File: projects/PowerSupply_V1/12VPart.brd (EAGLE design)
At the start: 49.5 x 58.4 mm, 24 parts, among them IC1 LM2596T, IC2 LM2596T, X1 IN, X2 OUT

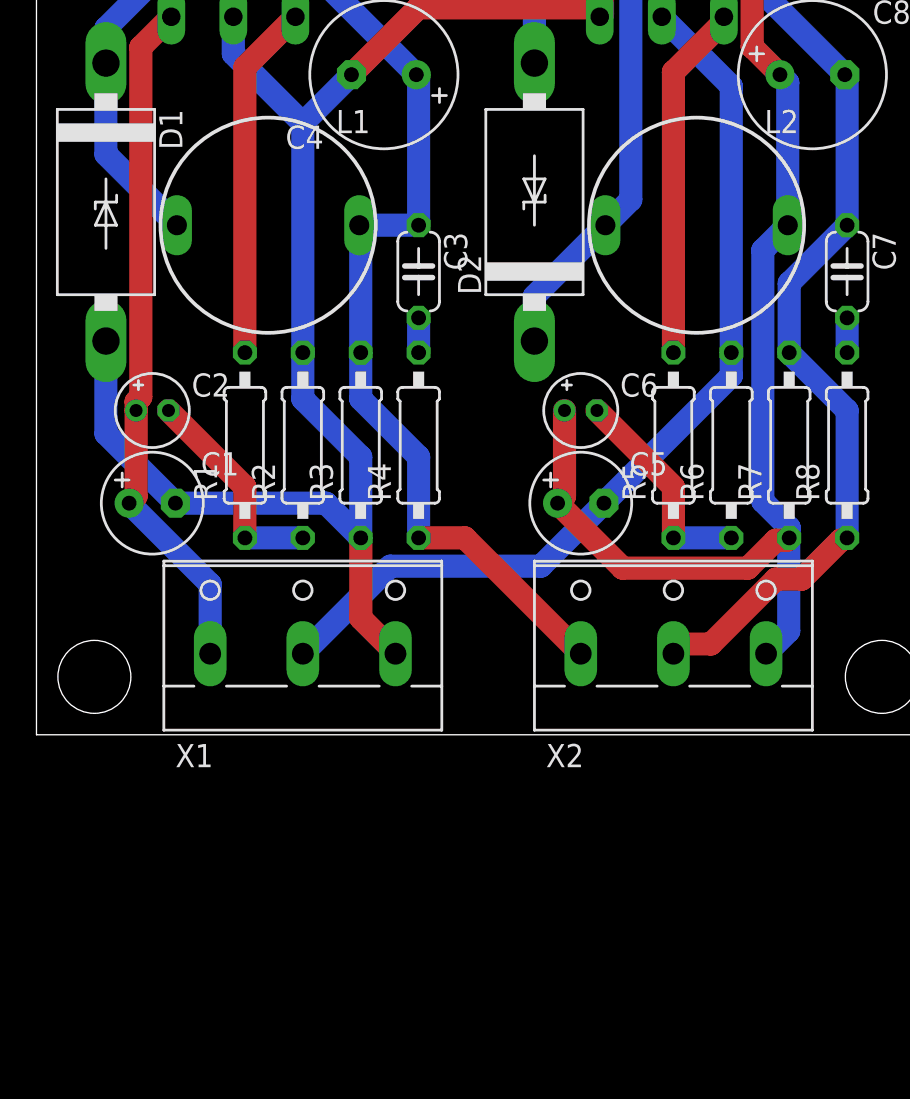
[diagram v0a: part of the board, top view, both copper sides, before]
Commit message: refactor(12v): schematics changed
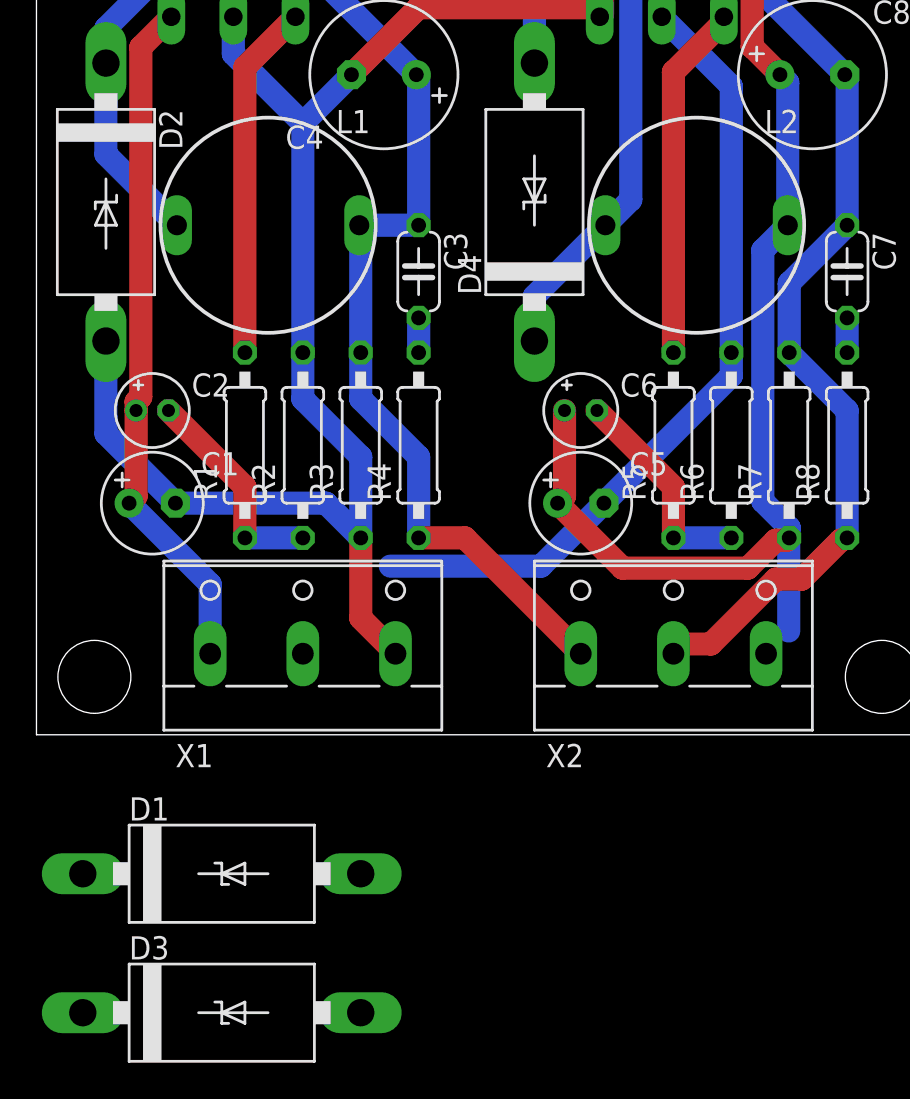
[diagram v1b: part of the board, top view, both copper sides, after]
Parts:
- added D3, D4: 1N5822, diode:C4111-15
- moved D1 37.4 mm to (10.2, -7.62), turned to 0 degrees
- moved D2 23.5 mm to (3.81, 29.2), turned to 270 degrees
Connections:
- net +24V: now also D1.C
- net -12V: now also D4.A, X2.3; no longer D2.A, X2.2
- net -24V: now also D3.C, X1.3; no longer X1.2
- net GND: now also D2.A, D3.A, X1.2, X2.2; no longer X1.3, X2.3
- net N$2: now also D4.C; no longer D2.C
- net N$3: now also D2.C; no longer D1.C
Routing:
- net -24V: track 51.1 -> 44.3 mm
- net GND: track 155.8 -> 154.0 mm
- net -12V: track 67.5 -> 66.8 mm
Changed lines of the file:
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@@
 <attribute name="VALUE" x="40.259" y="33.147" size="1.27" layer="27" ratio="10"/>
 </element>
-<element name="D1" library="diode" library_urn="urn:adsk.eagle:library:210" package="C4111-15" package3d_urn="urn:adsk.eagle:package:43355/2" value="1N5822" x="3.81" y="29.21" smashed="yes" rot="R270">
+<element name="D2" library="diode" library_urn="urn:adsk.eagle:library:210" package="C4111-15" package3d_urn="urn:adsk.eagle:package:43355/2" value="1N5822" x="3.81" y="29.21" smashed="yes" rot="R270">
 <attribute name="NAME" x="6.731" y="34.29" size="1.27" layer="25" ratio="10" rot="R270"/>
 <attribute name="POPULARITY" value="0" x="-25.4" y="-16.51" size="1.778" layer="27" rot="R270" display="off"/>
 <attribute name="VALUE" x="1.651" y="31.75" size="1.27" layer="27" ratio="10" rot="R270"/>
 </element>
-<element name="D2" library="diode" library_urn="urn:adsk.eagle:library:210" package="C4111-15" package3d_urn="urn:adsk.eagle:package:43355/2" value="1N5822" x="27.305" y="29.21" smashed="yes" rot="R90">
+<element name="D4" library="diode" library_urn="urn:adsk.eagle:library:210" package="C4111-15" package3d_urn="urn:adsk.eagle:package:43355/2" value="1N5822" x="27.305" y="29.21" smashed="yes" rot="R90">
 <attribute name="NAME" x="24.384" y="24.13" size="1.27" layer="25" ratio="10" rot="R90"/>
 <attribute name="POPULARITY" value="0" x="65.405" y="52.07" size="1.778" layer="27" rot="R90" display="off"/>
@@
 <attribute name="VALUE" x="28.321" y="0.762" size="1.27" layer="27" ratio="10"/>
 </element>
+<element name="D1" library="diode" library_urn="urn:adsk.eagle:library:210" package="C4111-15" package3d_urn="urn:adsk.eagle:package:43355/2" value="1N5822" x="10.16" y="-7.62" smashed="yes">
+<attribute name="NAME" x="5.08" y="-4.699" size="1.27" layer="25" ratio="10"/>
+<attribute name="POPULARITY" value="0" x="10.16" y="-7.62" size="1.778" layer="27" display="off"/>
+<attribute name="VALUE" x="7.62" y="-9.779" size="1.27" layer="27" ratio="10"/>
+</element>
+<element name="D3" library="diode" library_urn="urn:adsk.eagle:library:210" package="C4111-15" package3d_urn="urn:adsk.eagle:package:43355/2" value="1N5822" x="10.16" y="-15.24" smashed="yes">
+<attribute name="NAME" x="5.08" y="-12.319" size="1.27" layer="25" ratio="10"/>
+<attribute name="POPULARITY" value="0" x="10.16" y="-15.24" size="1.778" layer="27" display="off"/>
+<attribute name="VALUE" x="7.62" y="-17.399" size="1.27" layer="27" ratio="10"/>
+</element>
 </elements>
 <signals>
 <signal name="GND">
-<contactref element="X1" pad="3"/>
 <contactref element="C1" pad="-"/>
 <contactref element="IC1" pad="3"/>
 <contactref element="R2" pad="2"/>
 <contactref element="R3" pad="1"/>
-<contactref element="D1" pad="A"/>
-<contactref element="X2" pad="3"/>
+<contactref element="D2" pad="A"/>
 <contactref element="L2" pad="2"/>
 <contactref element="R7" pad="1"/>
@@
 <contactref element="C6" pad="+"/>
 <contactref element="IC2" pad="1"/>
-<wire x1="40.005" y1="4.445" x2="41.2496" y2="5.6896" width="1.27" layer="16"/>
 <wire x1="17.78" y1="6.4008" x2="17.78" y2="10.795" width="1.27" layer="1"/>
-<wire x1="19.685" y1="4.445" x2="19.685" y2="4.4958" width="1.27" layer="1"/>
 <wire x1="19.685" y1="4.4958" x2="17.78" y2="6.4008" width="1.27" layer="1"/>
 <wire x1="40.5384" y1="10.668" x2="41.148" y2="10.668" width="1.27" layer="1"/>
@@
 <wire x1="31.0388" y1="39.5224" x2="31.0388" y2="44.9393875" width="1.27" layer="1"/>
 <wire x1="31.9464125" y1="45.847" x2="36.6335875" y2="45.847" width="1.27" layer="1"/>
+<contactref element="X1" pad="2"/>
+<contactref element="X2" pad="2"/>
+<contactref element="D1" pad="A"/>
+<contactref element="D3" pad="A"/>
+<wire x1="41.2496" y1="5.6896" x2="34.925" y2="4.445" width="0" layer="19" extent="16-16"/>
+<wire x1="14.605" y1="4.445" x2="19.685" y2="4.4958" width="0" layer="19" extent="1-1"/>
+<wire x1="17.78" y1="-7.62" x2="19.685" y2="4.4958" width="0" layer="19" extent="1-1"/>
+<wire x1="17.78" y1="-15.24" x2="17.78" y2="-7.62" width="0" layer="19" extent="1-1"/>
 </signal>
 <signal name="N$3">
 <contactref element="IC1" pad="2"/>
-<contactref element="D1" pad="C"/>
+<contactref element="D2" pad="C"/>
 <contactref element="L1" pad="1"/>
 <wire x1="7.7" y1="27.94" x2="3.81" y2="31.83" width="1.27" layer="16"/>
@@
 <contactref element="L2" pad="1"/>
 <contactref element="IC2" pad="2"/>
-<contactref element="D2" pad="C"/>
+<contactref element="D4" pad="C"/>
 <wire x1="31.195" y1="27.94" x2="27.305" y2="24.05" width="1.27" layer="16"/>
 <wire x1="27.305" y1="24.05" x2="27.305" y2="21.59" width="1.27" layer="16"/>
@@
 </signal>
 <signal name="-12V">
-<contactref element="X2" pad="2"/>
 <contactref element="C8" pad="-"/>
 <contactref element="IC2" pad="4"/>
@@
 <contactref element="R8" pad="1"/>
 <contactref element="C7" pad="1"/>
-<contactref element="D2" pad="A"/>
+<contactref element="D4" pad="A"/>
 <wire x1="40.5384" y1="8.5344" x2="36.9824" y2="4.9784" width="1.27" layer="1"/>
 <wire x1="41.9608" y1="8.5344" x2="40.5384" y2="8.5344" width="1.27" layer="1"/>
@@
 <wire x1="44.0944" y1="10.668" x2="44.45" y2="10.795" width="1.27" layer="1"/>
 <wire x1="36.9824" y1="4.9784" x2="35.4584" y2="4.9784" width="1.27" layer="1"/>
-<wire x1="35.4584" y1="4.9784" x2="34.925" y2="4.445" width="1.27" layer="1"/>
 <wire x1="27.305" y1="36.83" x2="27.305" y2="41.2055875" width="1.27" layer="16"/>
 <wire x1="27.305" y1="41.2055875" x2="31.9464125" y2="45.847" width="1.27" layer="16"/>
@@
 <wire x1="41.275" y1="20.955" x2="44.45" y2="17.78" width="1.27" layer="16"/>
 <wire x1="44.45" y1="17.78" x2="44.45" y2="10.795" width="1.27" layer="16"/>
+<contactref element="X2" pad="3"/>
+<wire x1="35.4584" y1="4.9784" x2="40.005" y2="4.445" width="0" layer="19" extent="1-1"/>
 </signal>
 <signal name="+24V">
@@
 <wire x1="5.08" y1="12.7" x2="9.525" y2="8.255" width="1.27" layer="16"/>
 <wire x1="9.525" y1="8.255" x2="9.525" y2="4.445" width="1.27" layer="16"/>
+<contactref element="D1" pad="C"/>
+<wire x1="2.54" y1="-7.62" x2="9.525" y2="4.445" width="0" layer="19" extent="1-1"/>
 </signal>
 <signal name="-24V">
-<contactref element="X1" pad="2"/>
 <contactref element="C5" pad="-"/>
 <contactref element="R6" pad="2"/>
 <contactref element="IC2" pad="3"/>
 <wire x1="19.4056" y1="9.2456" x2="27.6606" y2="9.2456" width="1.27" layer="16"/>
-<wire x1="19.4056" y1="9.2456" x2="14.605" y2="4.445" width="1.27" layer="16"/>
 <wire x1="31.115" y1="12.7" x2="38.1" y2="19.685" width="1.27" layer="16"/>
 <wire x1="38.1" y1="19.685" x2="38.1" y2="20.955" width="1.27" layer="16"/>
@@
 <wire x1="34.29" y1="39.37" x2="38.1" y2="35.56" width="1.27" layer="16"/>
 <wire x1="38.1" y1="35.56" x2="38.1" y2="20.955" width="1.27" layer="16"/>
+<contactref element="X1" pad="3"/>
+<contactref element="D3" pad="C"/>
+<wire x1="19.685" y1="4.445" x2="19.4056" y2="9.2456" width="0" layer="19" extent="16-16"/>
+<wire x1="2.54" y1="-15.24" x2="19.685" y2="4.445" width="0" layer="19" extent="1-1"/>
 </signal>
 <signal name="N$4">

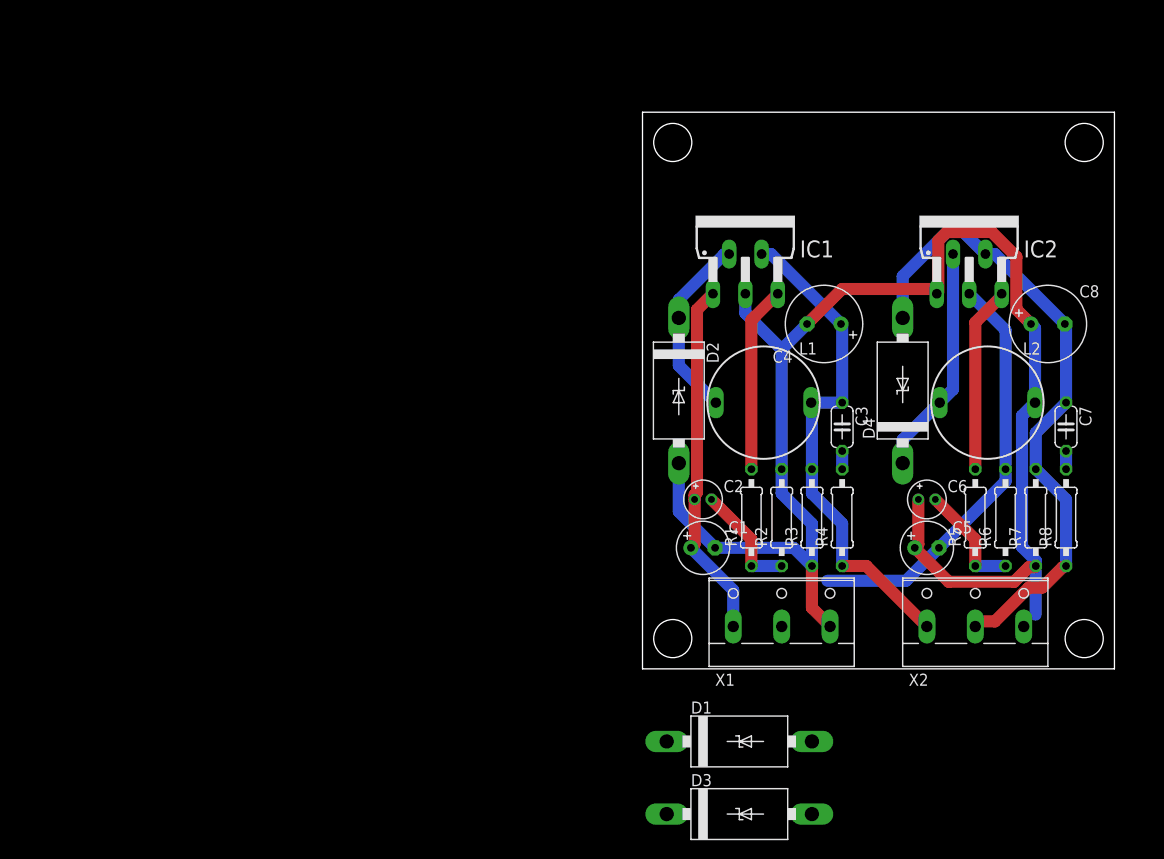
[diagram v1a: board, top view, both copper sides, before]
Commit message: refactor(1v): routing changed
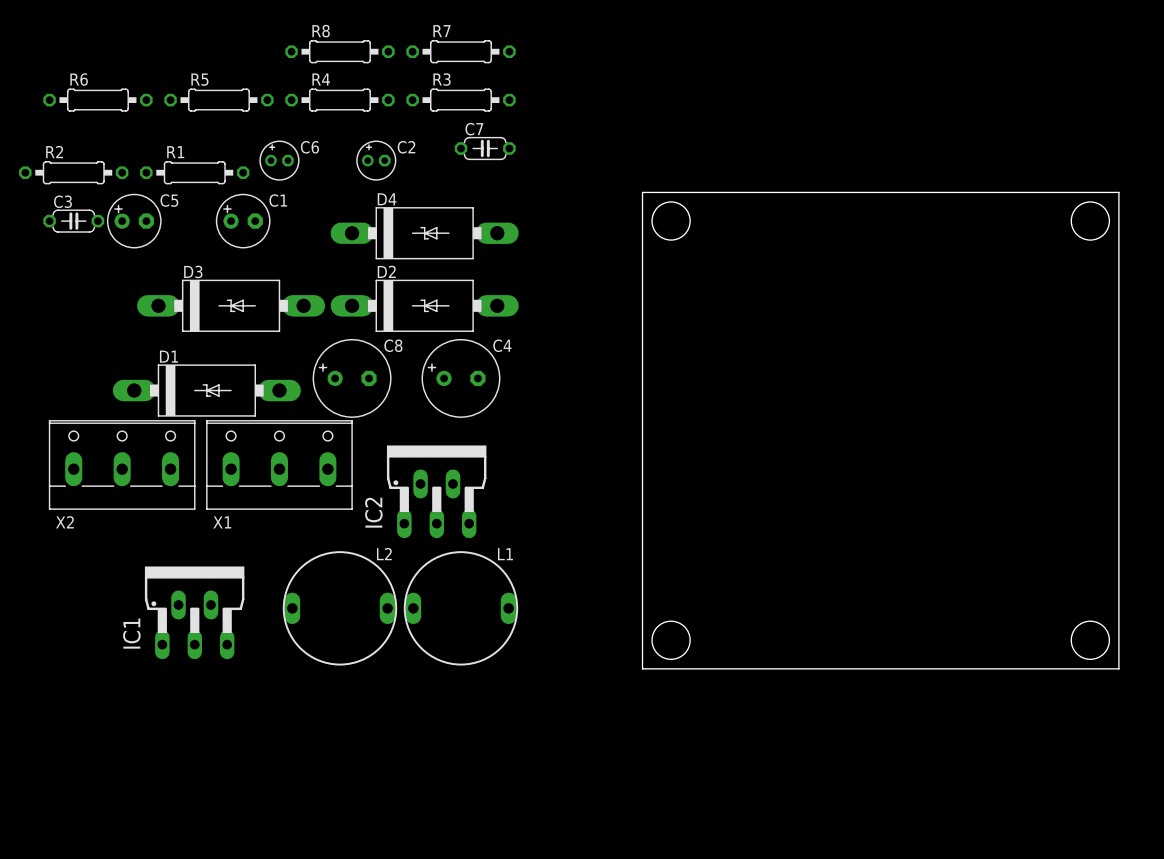
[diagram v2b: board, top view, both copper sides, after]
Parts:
- moved R6 104.8 mm to (-57.1, 59.7), turned to 0 degrees
- moved X2 91.0 mm to (-54.6, 21.6)
- moved R5 90.7 mm to (-44.5, 59.7), turned to 0 degrees
- moved R8 90.5 mm to (-31.8, 64.8), turned to 0 degrees
- moved C5 90.0 mm to (-53.3, 47.0)
- moved C3 83.5 mm to (-59.7, 47.0), turned to 0 degrees
- moved R2 82.6 mm to (-59.7, 52.1), turned to 0 degrees
- moved R7 77.7 mm to (-19.1, 64.8), turned to 0 degrees
- moved C6 76.7 mm to (-38.1, 53.3)
- moved D3 75.4 mm to (-43.2, 38.1)
- moved C8 73.2 mm to (-30.5, 30.5)
- moved L2 71.3 mm to (-31.8, 6.35)
- moved R1 68.7 mm to (-47.0, 52.1), turned to 0 degrees
- moved R4 68.5 mm to (-31.8, 59.7), turned to 0 degrees
- moved IC1 68.5 mm to (-47.0, 7.62)
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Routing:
- net GND: track 154.0 -> 0.00 mm
- net -12V: track 66.8 -> 0.00 mm
- net +12V: track 52.9 -> 0.00 mm
- net -24V: track 44.3 -> 0.00 mm
- net +24V: track 37.7 -> 0.00 mm
- net N$2: track 24.1 -> 0.00 mm
- net N$3: track 19.7 -> 0.00 mm
- net N$7: track 19.6 -> 0.00 mm
- net N$4: track 19.6 -> 0.00 mm
- net N$8: track 11.9 -> 0.00 mm
- net N$6: track 11.9 -> 0.00 mm
- net N$5: track 1.91 -> 0.00 mm
- net N$1: track 1.91 -> 0.00 mm
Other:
- board size 49.5 x 58.4 mm -> 50 x 50 mm

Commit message: refactor(all): schematics and routing changed
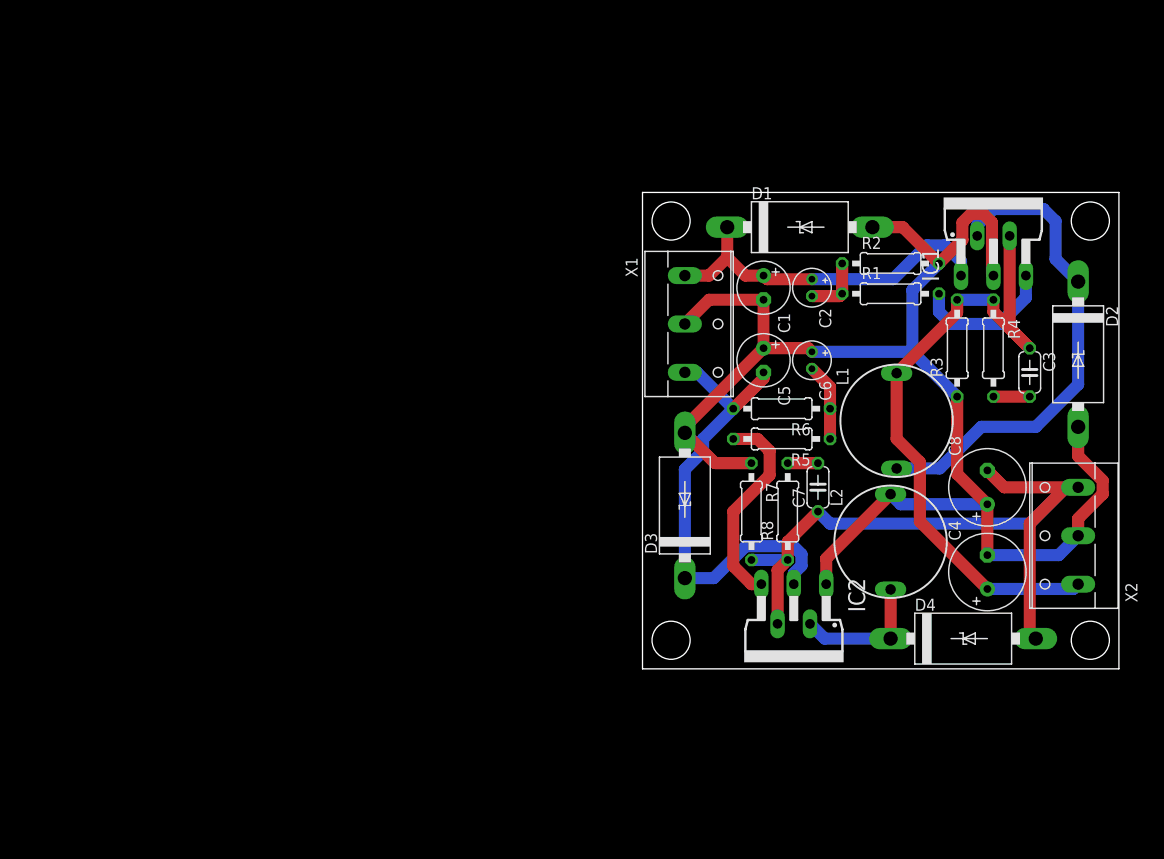
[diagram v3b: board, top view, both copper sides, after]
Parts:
- moved C3 101.6 mm to (40.6, 31.1), turned to 270 degrees
- moved X2 100.0 mm to (45.1, 14.0), turned to 90 degrees
- moved IC1 92.3 mm to (36.8, 46.4)
- moved R2 86.3 mm to (26.0, 42.5)
- moved R6 78.7 mm to (14.6, 27.3), turned to 180 degrees
- moved R1 74.1 mm to (26.0, 39.4)
- moved R4 73.4 mm to (36.8, 33.7), turned to 270 degrees
- moved D4 70.7 mm to (33.7, 3.17)
- moved R5 68.9 mm to (14.6, 24.1), turned to 180 degrees
- moved D2 68.8 mm to (45.7, 33.0), turned to 270 degrees
- moved C8 67.6 mm to (36.2, 19.1), turned to 90 degrees
- moved C5 67.6 mm to (12.7, 32.4), turned to 270 degrees
- moved R8 67.4 mm to (15.2, 16.5), turned to 90 degrees
- moved D1 64.5 mm to (16.5, 46.4)
- moved C6 59.7 mm to (17.8, 32.4), turned to 270 degrees
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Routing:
- net GND: track 0.00 -> 155.9 mm
- net -12V: track 0.00 -> 76.0 mm
- net +12V: track 0.00 -> 69.8 mm
- net N$3: track 0.00 -> 51.4 mm
- net -24V: track 0.00 -> 49.1 mm
- net +24V: track 0.00 -> 38.2 mm
- net N$7: track 0.00 -> 21.7 mm
- net N$4: track 0.00 -> 15.0 mm
- net N$2: track 0.00 -> 14.3 mm
- net N$8: track 0.00 -> 8.16 mm
- net N$6: track 0.00 -> 6.46 mm
- net N$1: track 0.00 -> 3.81 mm
- net N$5: track 0.00 -> 3.17 mm
